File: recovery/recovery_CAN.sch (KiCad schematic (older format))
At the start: 5 parts

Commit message: add raven4 and stratologer altimeters
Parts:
- added A?: StratoLoggerCF, symbol recovery_CAN-cache:StratoLoggerCF
- added A?: Raven4, symbol recovery_CAN-cache:Raven4
- added J?: Conn_01x05_Female, symbol Connector:Conn_01x05_Female
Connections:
- net labels added: ICSPCLK, ICSPDAT, ~MCLR
- wire segments 20 -> 27
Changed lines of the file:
@@
 EESchema Schematic File Version 4
+LIBS:recovery_CAN-cache
 EELAYER 26 0
 EELAYER END
@@
 	3000 3750 3400 3750
 Connection ~ 3000 3800
+$Comp
+L Connector:Conn_01x05_Female J?
+U 1 1 5D959CC4
+P 1700 1300
+F 0 "J?" H 1594 875 50  0000 C CNN
+F 1 "Conn_01x05_Female" H 1594 966 50  0000 C CNN
+F 2 "" H 1700 1300 50  0001 C CNN
+F 3 "~" H 1700 1300 50  0001 C CNN
+	1    1700 1300
+	-1   0    0    1
+$EndComp
+Text Label 2150 1100 0    50   ~ 0
+~MCLR
+Wire Wire Line
+	1900 1100 2150 1100
+$Comp
+L power:+5V #PWR?
+U 1 1 5D95A01E
+P 2500 1100
+F 0 "#PWR?" H 2500 950 50  0001 C CNN
+F 1 "+5V" H 2515 1273 50  0000 C CNN
+F 2 "" H 2500 1100 50  0001 C CNN
+F 3 "" H 2500 1100 50  0001 C CNN
+	1    2500 1100
+	1    0    0    -1
+$EndComp
+Wire Wire Line
+	1900 1200 2500 1200
+Wire Wire Line
+	2500 1200 2500 1100
+$Comp
+L power:GND #PWR?
+U 1 1 5D95A4EB
+P 2500 1700
+F 0 "#PWR?" H 2500 1450 50  0001 C CNN
+F 1 "GND" H 2505 1527 50  0000 C CNN
+F 2 "" H 2500 1700 50  0001 C CNN
+F 3 "" H 2500 1700 50  0001 C CNN
+	1    2500 1700
+	1    0    0    -1
+$EndComp
+Wire Wire Line
+	1900 1300 2500 1300
+Wire Wire Line
+	2500 1300 2500 1700
+Text Label 2150 1500 0    50   ~ 0
+ICSPCLK
+Text Label 2150 1400 0    50   ~ 0
+ICSPDAT
+Wire Wire Line
+	2150 1400 1900 1400
+Wire Wire Line
+	2150 1500 1900 1500
+Text Label 6600 2600 0    50   ~ 0
+ICSPDAT
+Text Label 6600 2700 0    50   ~ 0
+ICSPCLK
+Text Label 5150 2500 2    50   ~ 0
+~MCLR
+$Comp
+L recovery_CAN-cache:StratoLoggerCF A?
+U 1 1 5D9977AA
+P 8550 1650
+F 0 "A?" H 8800 2365 50  0000 C CNN
+F 1 "StratoLoggerCF" H 8800 2274 50  0000 C CNN
+F 2 "" H 8550 1650 50  0001 C CNN
+F 3 "" H 8550 1650 50  0001 C CNN
+	1    8550 1650
+	1    0    0    -1
+$EndComp
+$Comp
+L recovery_CAN-cache:Raven4 A?
+U 1 1 5D9983F7
+P 8500 3150
+F 0 "A?" H 8500 3565 50  0000 C CNN
+F 1 "Raven4" H 8500 3474 50  0000 C CNN
+F 2 "" H 8550 3150 50  0001 C CNN
+F 3 "" H 8550 3150 50  0001 C CNN
+	1    8500 3150
+	1    0    0    -1
+$EndComp
 $EndSCHEMATC

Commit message: split into seperate sheets, add majority of support and arming circutry
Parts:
- removed A?: StratoLoggerCF, symbol recovery_CAN-cache:StratoLoggerCF
- removed A?: Raven4, symbol recovery_CAN-cache:Raven4
- added D? (x3): LED, symbol Device:LED
- added R? (x3): 330R, symbol Device:R_US
- added U?: MCP2562, symbol canhw:MCP2562
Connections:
- net labels added: LED1, LED2, LED3
- wire segments 27 -> 47
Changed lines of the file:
@@
 $Descr A4 11693 8268
 encoding utf-8
-Sheet 1 1
+Sheet 1 3
 Title "recovery_CAN"
 Date ""
@@
 Text Label 5150 2500 2    50   ~ 0
 ~MCLR
-$Comp
-L recovery_CAN-cache:StratoLoggerCF A?
-U 1 1 5D9977AA
-P 8550 1650
-F 0 "A?" H 8800 2365 50  0000 C CNN
-F 1 "StratoLoggerCF" H 8800 2274 50  0000 C CNN
-F 2 "" H 8550 1650 50  0001 C CNN
-F 3 "" H 8550 1650 50  0001 C CNN
-	1    8550 1650
-	1    0    0    -1
-$EndComp
-$Comp
-L recovery_CAN-cache:Raven4 A?
-U 1 1 5D9983F7
-P 8500 3150
-F 0 "A?" H 8500 3565 50  0000 C CNN
-F 1 "Raven4" H 8500 3474 50  0000 C CNN
-F 2 "" H 8550 3150 50  0001 C CNN
-F 3 "" H 8550 3150 50  0001 C CNN
-	1    8500 3150
-	1    0    0    -1
-$EndComp
+$Sheet
+S 9150 3650 1950 1200
+U 5DA13C95
+F0 "power" 50
+F1 "power.sch" 50
+F2 "CURR_AMP" I L 9150 4050 50
+F3 "VBAT1" I L 9150 4300 50
+F4 "VBAT2" I L 9150 4450 50
+$EndSheet
+$Sheet
+S 9050 2050 1100 1150
+U 5DA13D99
+F0 "altimeters" 50
+F1 "altimeters.sch" 50
+F2 "SL_TX" I L 9050 2300 50
+F3 "SL_ARM" I L 9050 2550 50
+F4 "A2_ARM" I L 9050 2750 50
+F5 "A2_DROGUE" I R 10150 2250 50
+F6 "A2_MAIN" I R 10150 2400 50
+F7 "A1_DROGUE" I R 10150 2600 50
+F8 "A1_MAIN" I R 10150 2750 50
+$EndSheet
+$Comp
+L Device:LED D?
+U 1 1 5DAA8959
+P 5150 5750
+F 0 "D?" V 5095 5828 50  0000 L CNN
+F 1 "LED" V 5186 5828 50  0000 L CNN
+F 2 "" H 5150 5750 50  0001 C CNN
+F 3 "~" H 5150 5750 50  0001 C CNN
+	1    5150 5750
+	0    1    1    0
+$EndComp
+$Comp
+L Device:LED D?
+U 1 1 5DAA89D1
+P 4800 5750
+F 0 "D?" V 4745 5828 50  0000 L CNN
+F 1 "LED" V 4836 5828 50  0000 L CNN
+F 2 "" H 4800 5750 50  0001 C CNN
+F 3 "~" H 4800 5750 50  0001 C CNN
+	1    4800 5750
+	0    1    1    0
+$EndComp
+$Comp
+L Device:LED D?
+U 1 1 5DAA8A2E
+P 4450 5750
+F 0 "D?" V 4395 5828 50  0000 L CNN
+F 1 "LED" V 4486 5828 50  0000 L CNN
+F 2 "" H 4450 5750 50  0001 C CNN
+F 3 "~" H 4450 5750 50  0001 C CNN
+	1    4450 5750
+	0    1    1    0
+$EndComp
+$Comp
+L power:+5V #PWR?
+U 1 1 5DAA8A9F
+P 4800 5150
+F 0 "#PWR?" H 4800 5000 50  0001 C CNN
+F 1 "+5V" H 4815 5323 50  0000 C CNN
+F 2 "" H 4800 5150 50  0001 C CNN
+F 3 "" H 4800 5150 50  0001 C CNN
+	1    4800 5150
+	1    0    0    -1
+$EndComp
+Wire Wire Line
+	4450 5600 4450 5350
+Wire Wire Line
+	4450 5350 4800 5350
+Wire Wire Line
+	5150 5350 5150 5600
+Wire Wire Line
+	4800 5350 4800 5600
+Connection ~ 4800 5350
+Wire Wire Line
+	4800 5350 5150 5350
+Wire Wire Line
+	4800 5350 4800 5150
+$Comp
+L Device:R_US R?
+U 1 1 5DAA98F4
+P 5150 6050
+F 0 "R?" H 5218 6096 50  0000 L CNN
+F 1 "330R" H 5218 6005 50  0000 L CNN
+F 2 "" V 5190 6040 50  0001 C CNN
+F 3 "~" H 5150 6050 50  0001 C CNN
+	1    5150 6050
+	1    0    0    -1
+$EndComp
+$Comp
+L Device:R_US R?
+U 1 1 5DAA9942
+P 4800 6050
+F 0 "R?" H 4868 6096 50  0000 L CNN
+F 1 "330R" H 4868 6005 50  0000 L CNN
+F 2 "" V 4840 6040 50  0001 C CNN
+F 3 "~" H 4800 6050 50  0001 C CNN
+	1    4800 6050
+	1    0    0    -1
+$EndComp
+$Comp
+L Device:R_US R?
+U 1 1 5DAA9AA5
+P 4450 6050
+F 0 "R?" H 4518 6096 50  0000 L CNN
+F 1 "330R" H 4518 6005 50  0000 L CNN
+F 2 "" V 4490 6040 50  0001 C CNN
+F 3 "~" H 4450 6050 50  0001 C CNN
+	1    4450 6050
+	1    0    0    -1
+$EndComp
+$Comp
+L canhw:MCP2562 U?
+U 1 1 5DAA9FEB
+P 1900 6450
+F 0 "U?" H 1875 6715 50  0000 C CNN
+F 1 "MCP2562" H 1875 6624 50  0000 C CNN
+F 2 "" H 1900 6450 50  0001 C CNN
+F 3 "http://hades.mech.northwestern.edu/images/5/5e/MCP2562.pdf" H 1900 6450 50  0001 C CNN
+	1    1900 6450
+	1    0    0    -1
+$EndComp
+$Comp
+L power:+5V #PWR?
+U 1 1 5DAAA5AA
+P 1200 6200
+F 0 "#PWR?" H 1200 6050 50  0001 C CNN
+F 1 "+5V" H 1215 6373 50  0000 C CNN
+F 2 "" H 1200 6200 50  0001 C CNN
+F 3 "" H 1200 6200 50  0001 C CNN
+	1    1200 6200
+	1    0    0    -1
+$EndComp
+$Comp
+L power:GND #PWR?
+U 1 1 5DAAA7CF
+P 2550 6950
+F 0 "#PWR?" H 2550 6700 50  0001 C CNN
+F 1 "GND" H 2555 6777 50  0000 C CNN
+F 2 "" H 2550 6950 50  0001 C CNN
+F 3 "" H 2550 6950 50  0001 C CNN
+	1    2550 6950
+	1    0    0    -1
+$EndComp
+Wire Wire Line
+	2350 6450 2550 6450
+Wire Wire Line
+	2550 6450 2550 6750
+Wire Wire Line
+	2350 6750 2550 6750
+Connection ~ 2550 6750
+Wire Wire Line
+	2550 6750 2550 6950
+Wire Wire Line
+	1400 6450 1200 6450
+Wire Wire Line
+	1400 6550 1200 6550
+Wire Wire Line
+	1200 6200 1200 6450
+Connection ~ 1200 6450
+Wire Wire Line
+	1200 6450 1200 6550
+Text Label 5400 6300 0    50   ~ 0
+LED1
+Text Label 5400 6450 0    50   ~ 0
+LED2
+Text Label 5400 6600 0    50   ~ 0
+LED3
+Wire Wire Line
+	5150 6200 5150 6300
+Wire Wire Line
+	5150 6300 5400 6300
+Wire Wire Line
+	4800 6200 4800 6450
+Wire Wire Line
+	4800 6450 5400 6450
+Wire Wire Line
+	4450 6200 4450 6600
+Wire Wire Line
+	4450 6600 5400 6600
+Text Label 6600 3600 0    50   ~ 0
+LED1
+Text Label 6600 3500 0    50   ~ 0
+LED2
+Text Label 6600 3400 0    50   ~ 0
+LED3
 $EndSCHEMATC

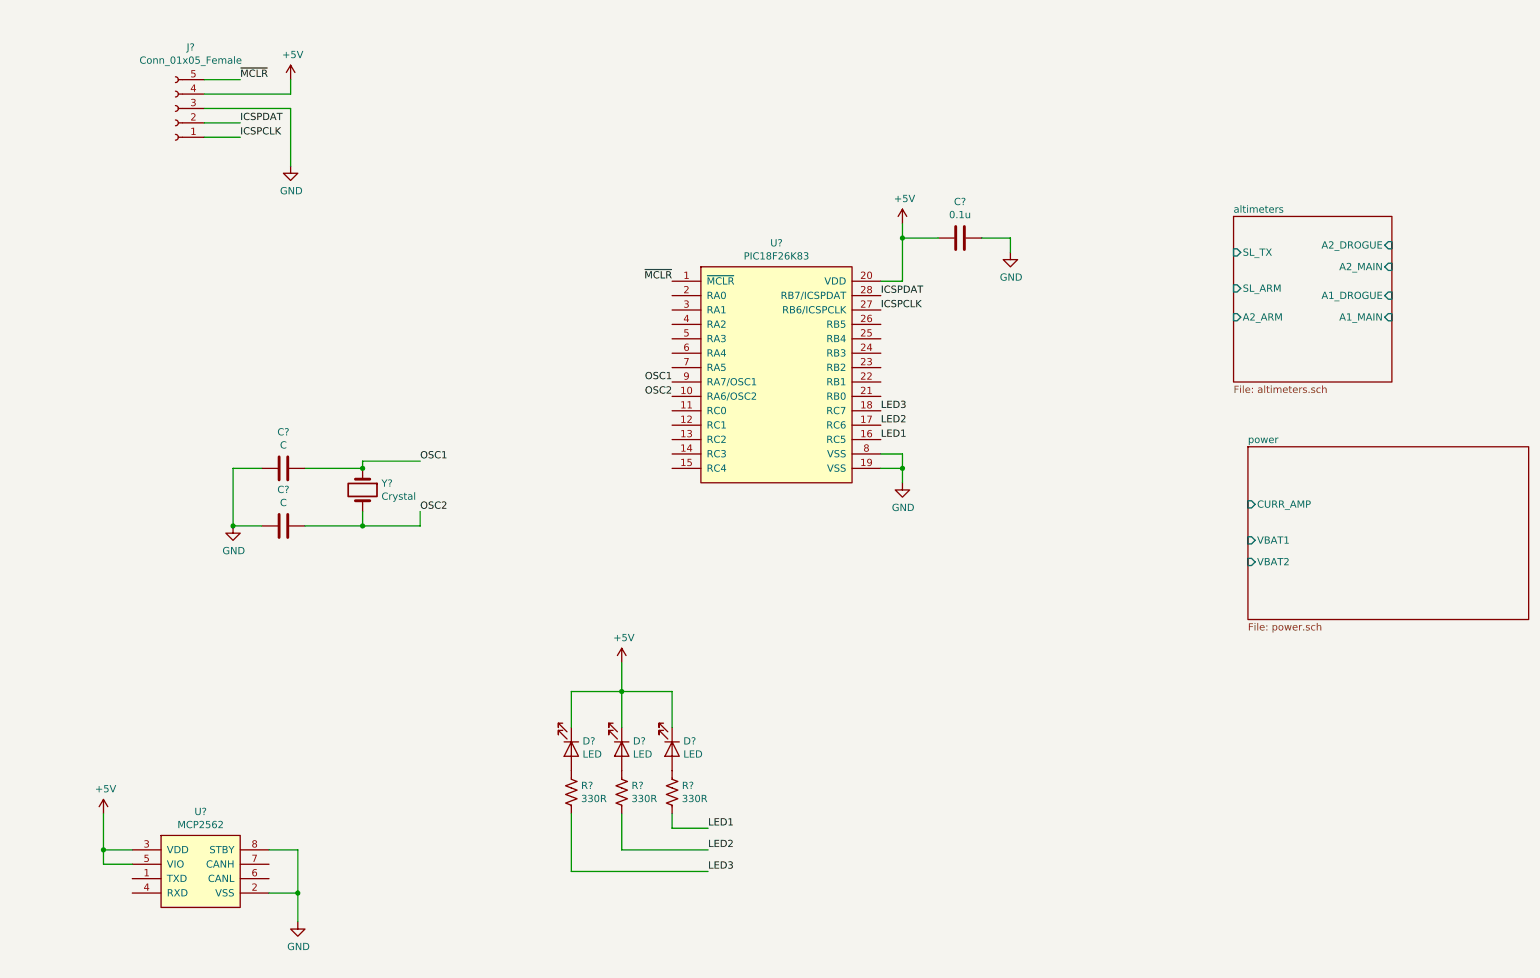
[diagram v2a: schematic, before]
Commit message: finnish adding altimeter and other support electronics
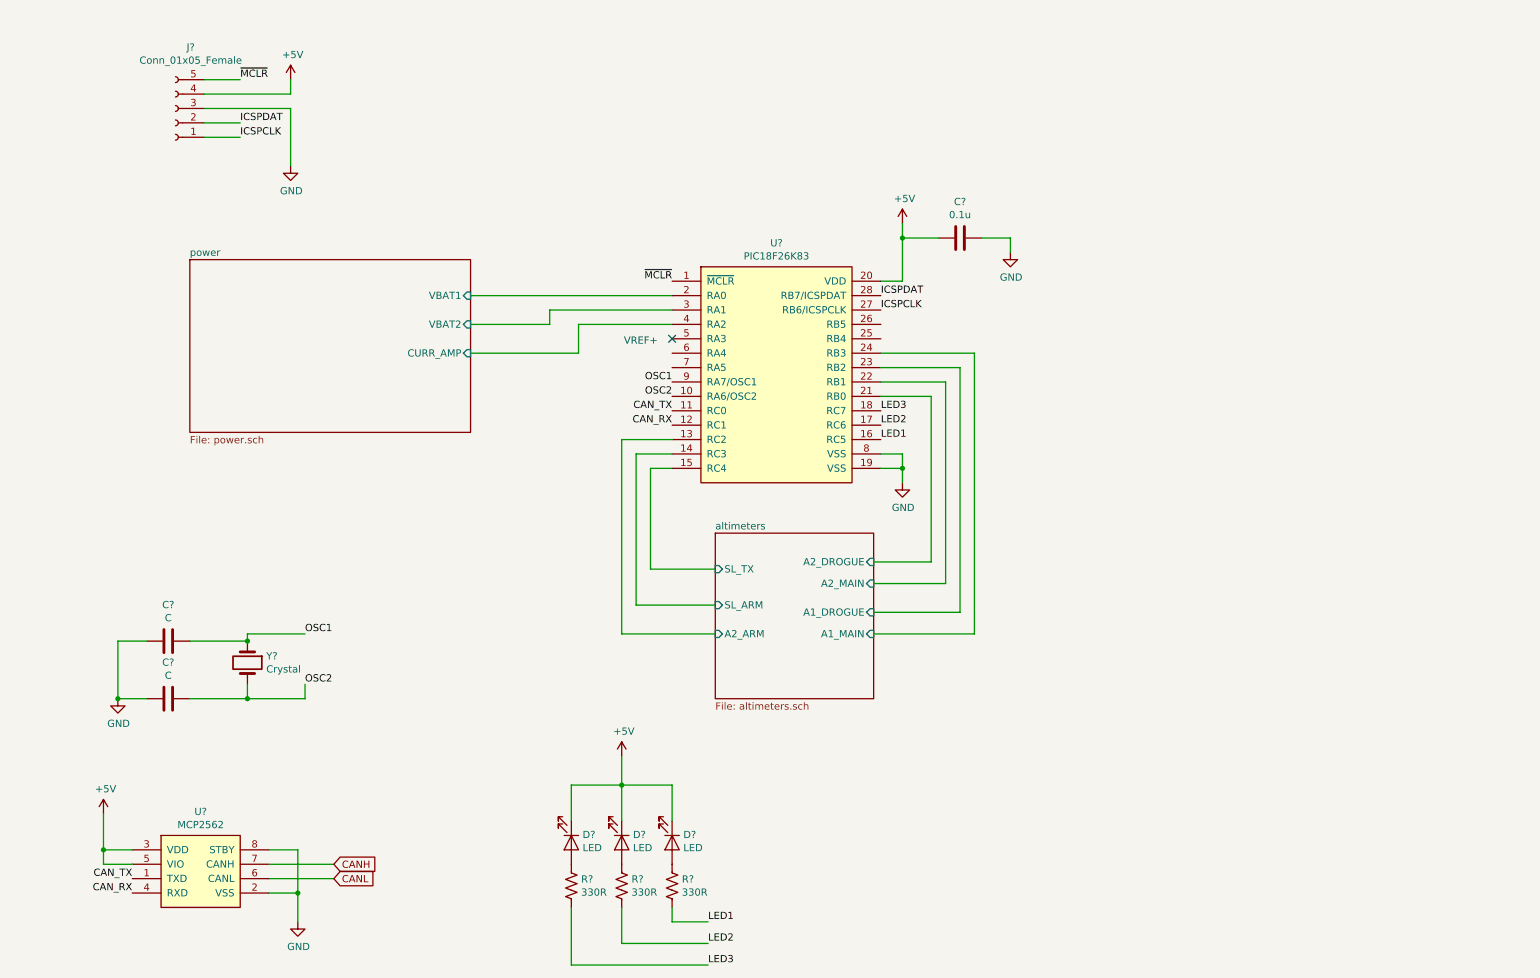
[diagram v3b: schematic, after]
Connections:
- net altimeters/A1_DROGUE: now also U?.23 (RB2)
- net altimeters/A1_MAIN: now also U?.24 (RB3)
- net altimeters/A2_ARM: now also U?.13 (RC2)
- net altimeters/A2_DROGUE: now also U?.21 (RB0)
- net altimeters/A2_MAIN: now also U?.22 (RB1)
- net altimeters/SL_ARM: now also U?.14 (RC3)
- net altimeters/SL_TX: now also U?.15 (RC4)
- net power/CURR_AMP: now also U?.4 (RA2)
- net power/VBAT1: now also U?.2 (RA0)
- net power/VBAT2: now also U?.3 (RA1)
- net CAN_TX: now reaches U?.11 (RC0)
- net CAN_TX: now also U?.1 (TXD)
- net CAN_RX: now reaches U?.12 (RC1)
- net CAN_RX: now also U?.4 (RXD)
- net CANL: now reaches U?.6 (CANL)
- net CANH: now reaches U?.7 (CANH)
- no-connect marks 0 -> 1
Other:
- note added: "VREF+"
- moved on the sheet: C?, D?, R?, Y?
